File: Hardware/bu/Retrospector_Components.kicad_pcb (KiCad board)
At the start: 4 copper layers, 60 x 110 mm, 145 parts, among them J1 SWD_Header, J2 Eurorack_10_pin_power, J3 Conn_01x08_Male, J4 Conn_01x08_Male, J5 Conn_01x08_Male, J6 Conn_01x08_Male, J7 USB_B_Micro, U1 STM32H743ZITx, U10 LM2675M-5, U11 TL072, U2 IS42S16800F-7TLI, U3 PCM5100APW, U4 SSI2164, U5 MCP6004, U6 MCP6004, U7 TL074, U8 LD1117-3.3-4Tab, Y1 8MHz 20pF

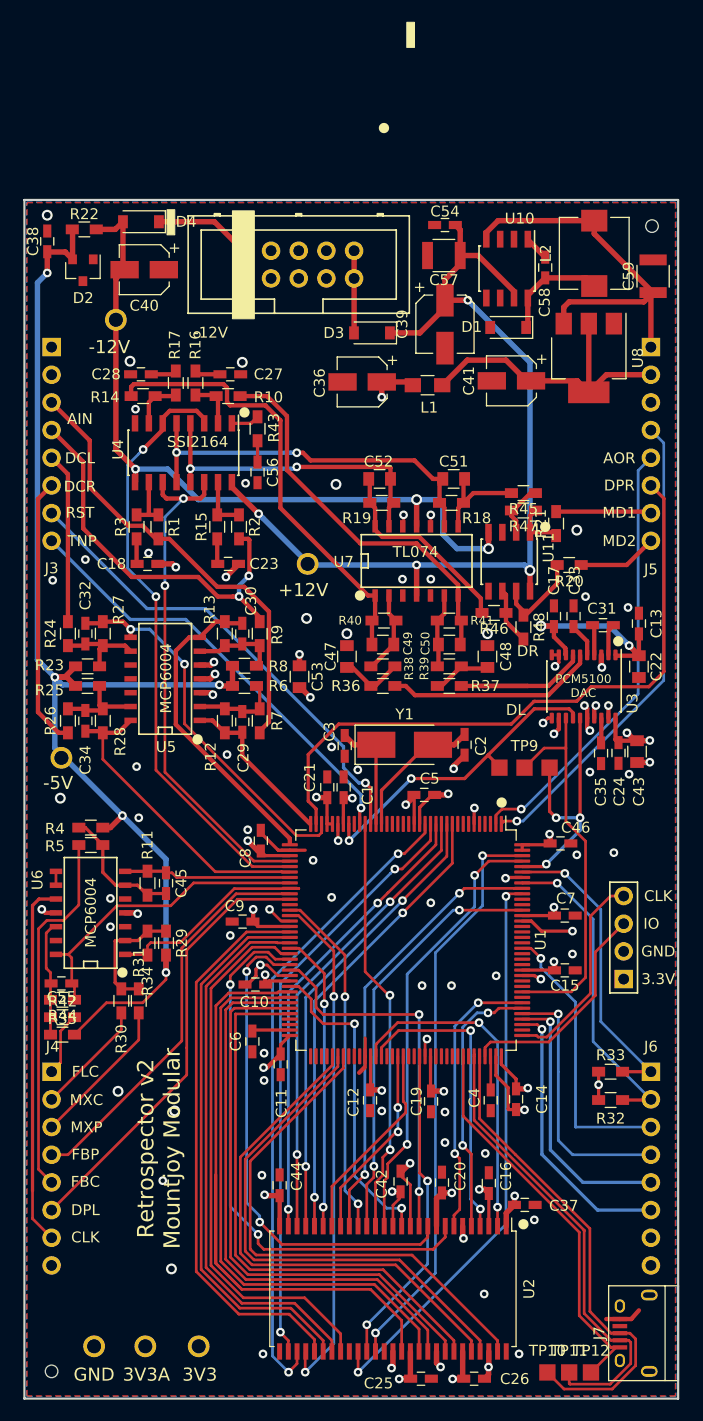
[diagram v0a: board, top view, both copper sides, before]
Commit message: Added some test code using SPI to control Toshiba LED controller
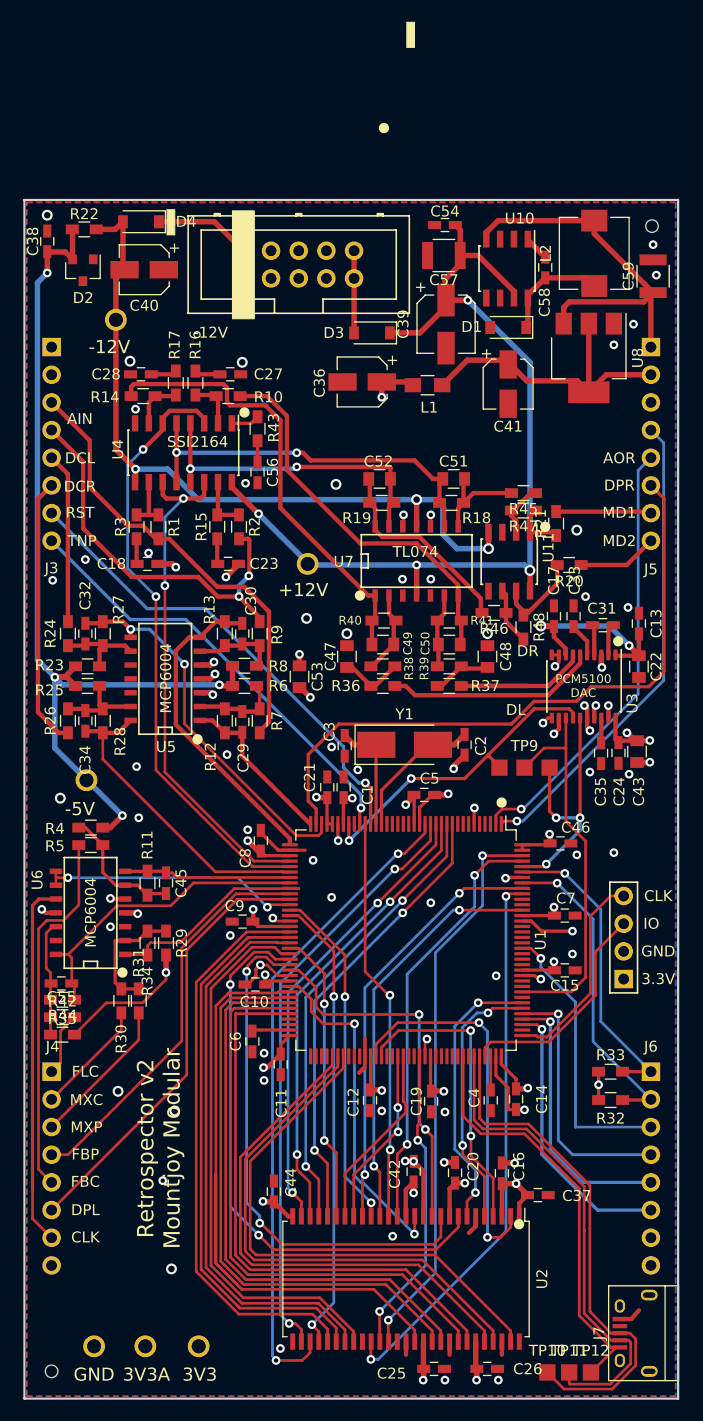
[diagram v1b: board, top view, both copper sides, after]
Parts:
- moved TP4 3.08 mm to (105.7, 103.2)
- moved C20 1.50 mm to (139.5, 139.3)
- moved U2 1.50 mm to (135.0, 149.0)
- moved C16 1.50 mm to (143.8, 139.3)
- moved C25 1.50 mm to (137.6, 157.3)
- moved C26 1.50 mm to (142.5, 157.3)
- moved C37 1.50 mm to (147.1, 141.3)
- moved C42 1.50 mm to (135.7, 139.2)
- moved C44 0.78 mm to (122.9, 141.0)
- moved C41 0.42 mm to (144.4, 66.9), turned to 270 degrees
- moved C39 0.10 mm to (138.7, 61.4)
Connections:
- U1 pad 127: /CLOCK_SCALED -> Net-(U1-Pad127)
- U1 pad 48: Net-(U1-Pad48) -> /CLOCK_SCALED
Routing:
- net /CLOCK_SCALED: track 1.27 -> 24.0 mm, vias 0 -> 2
- net /FMC_A6: track 47.1 -> 42.3 mm
- net /FMC_D0: track 30.8 -> 34.9 mm
- net /USB_VBUS: track 36.7 -> 39.1 mm
- net /USB_DM: track 42.8 -> 45.2 mm
- net /USB_DP: track 45.0 -> 47.3 mm
- net /FMC_D7: track 29.2 -> 31.4 mm
- net /FMC_D5: track 46.2 -> 48.2 mm
- net /FMC_SDCKE1: track 52.8 -> 51.2 mm
- net /FMC_SD~E1: track 40.7 -> 39.3 mm
- net /FMC_BA1: track 18.5 -> 17.1 mm
- net /FMC_SD~WE: track 38.4 -> 37.0 mm
- net /FMC_~BL0: track 40.5 -> 39.1 mm
- net /FMC_~BL1: track 53.1 -> 51.7 mm
- net /FMC_SDCLK: track 29.7 -> 28.3 mm
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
